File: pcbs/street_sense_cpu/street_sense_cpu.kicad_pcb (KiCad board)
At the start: 2 copper layers, 20 parts, among them J1 Conn_01x08, J10 Conn_01x06, J11 Conn_01x09, J13 Conn_01x02, J14 Conn_01x02, J3 Conn_01x06, J4 Conn_01x04, J5 Conn_01x02, J6 Conn_01x02, J7 Conn_01x08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

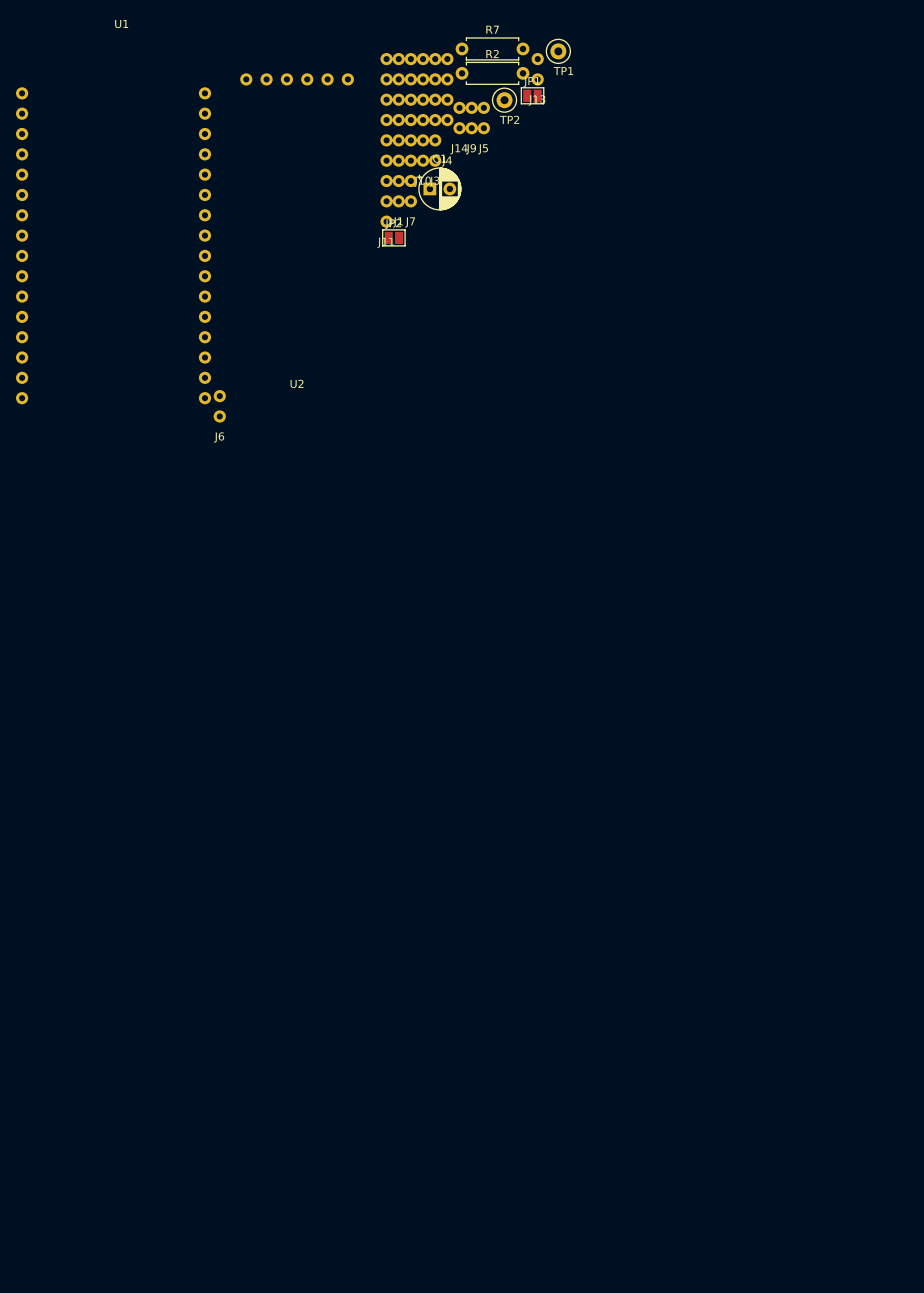
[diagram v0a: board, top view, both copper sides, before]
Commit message: updated CPU schematic
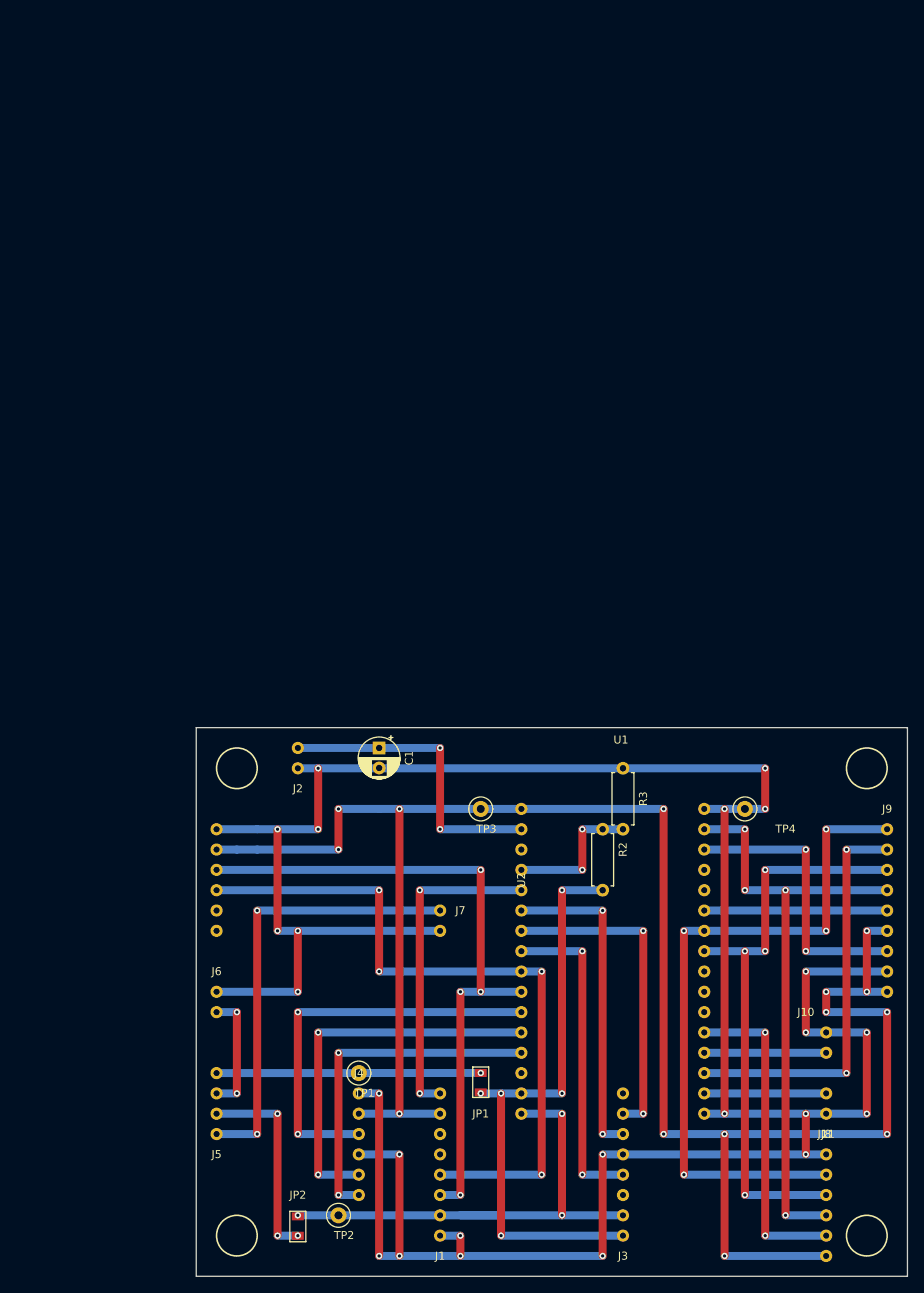
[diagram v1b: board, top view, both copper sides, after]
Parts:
- removed J13, J14: Conn_01x02, street-sense_footprints:connector_2pin
- removed R7: 100k, Resistor_THT:R_Axial_DIN0207_L6.3mm_D2.5mm_P7.62mm_Horizontal
- added J2: Conn_01x02, street_sense_footprints:connector_2pin, F.Cu at (114.3, 124.5)
- added J8: Conn_01x06, street_sense_footprints:connector_6pin, F.Cu at (180.3, 193.0)
- added R3: 100k, Resistor_THT:R_Axial_DIN0207_L6.3mm_D2.5mm_P7.62mm_Horizontal, F.Cu at (154.9, 129.5)
- added TP3: TestPoint, TestPoint:TestPoint_Loop_D2.50mm_Drill1.0mm, F.Cu at (137.2, 134.6)
- added TP4: TestPoint, TestPoint:TestPoint_Loop_D2.50mm_Drill1.0mm, F.Cu at (170.2, 134.6)
- J1: footprint street-sense_footprints:connector_8pin -> street_sense_footprints:connector_8pin
- J10: value Conn_01x06 -> Conn_01x02; footprint street-sense_footprints:connector_6pin -> street_sense_footprints:connector_2pin
- J11: value Conn_01x09 -> Conn_01x02; footprint street-sense_footprints:connector_9pin -> street_sense_footprints:connector_2pin
- J3: value Conn_01x06 -> Conn_01x08; footprint street-sense_footprints:connector_6pin -> street_sense_footprints:connector_8pin
- J4: value Conn_01x04 -> Conn_01x06; footprint street-sense_footprints:connector_4pin -> street_sense_footprints:connector_6pin
- J5: value Conn_01x02 -> Conn_01x04; footprint street-sense_footprints:connector_2pin -> street_sense_footprints:connector_4pin
- J6: footprint street-sense_footprints:connector_2pin -> street_sense_footprints:connector_2pin
- J7: value Conn_01x08 -> Conn_01x02; footprint street-sense_footprints:connector_8pin -> street_sense_footprints:connector_2pin
- J9: value Conn_01x02 -> Conn_01x09; footprint street-sense_footprints:connector_2pin -> street_sense_footprints:connector_9pin
- JP1, JP2: footprint Jumper:SolderJumper-2_P1.3mm_Open_Pad1.0x1.5mm -> street_sense_footprints:SolderJumper-2_P1.3mm_Open_Pad1.0x1.5mm
- R2: value 470k -> 68k
- U1: footprint street-sense_footprints:LolinD32 -> street_sense_footprints:LolinD32
- U2: footprint street-sense_footprints:DS3231_Module -> street_sense_footprints:DS3231_Module
- moved J4 147.5 mm to (121.9, 185.4), turned to 180 degrees
- moved TP2 140.9 mm to (119.4, 185.4)
- moved J11 140.5 mm to (180.3, 167.6)
- moved J10 138.8 mm to (180.3, 167.6), turned to 180 degrees
- moved J3 131.4 mm to (154.9, 167.6)
- moved TP1 130.1 mm to (121.9, 167.6)
- moved J1 129.4 mm to (132.1, 167.6)
- moved J9 126.7 mm to (188.0, 160.0), turned to 180 degrees
- moved JP2 125.3 mm to (114.3, 188.0), turned to 90 degrees
- moved J5 125.2 mm to (104.1, 165.1)
- moved JP1 122.3 mm to (137.2, 167.6), turned to 270 degrees
- moved U2 109.6 mm to (99.1, 147.3), turned to 90 degrees
- moved U1 109.1 mm to (154.9, 142.2)
- moved J7 106.5 mm to (132.1, 144.8)
- moved R2 96.1 mm to (152.4, 137.2), turned to 270 degrees
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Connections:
- J1 pad 1: Net-(J1-Pad1) -> /DRDY
- J1 pad 2: /PS_RX -> +3V3
- J1 pad 3: /PS_TX -> Net-(J1-Pad3)
- J1 pad 4: GND -> Net-(J1-Pad4)
- J1 pad 5: /PS_CTRL -> /SCL
- J1 pad 6: Net-(J1-Pad6) -> /SDA
- J1 pad 8: /USB -> GND
- J10 pad 1: +3V3 -> /ADVANCE
- J10 pad 2: /SD_CS -> GND
- J11 pad 1: +3V3 -> /SELECT
- J3 pad 1: /SCK -> Net-(J3-Pad1)
- J3 pad 2: /WS -> /PS_RX
- J3 pad 3: GND -> /PS_TX
- J3 pad 4: /SD -> GND
- J3 pad 5: +3V3 -> /PS_CTRL
- J3 pad 6: GND -> Net-(J3-Pad6)
- J4 pad 1: Net-(J4-Pad1) -> /M_SCK
- J4 pad 2: Net-(J4-Pad2) -> /M_WS
- J4 pad 3: Net-(J4-Pad3) -> GND
- J4 pad 4: Net-(J4-Pad4) -> /M_SD
- J5 pad 1: Net-(J4-Pad3) -> Net-(J5-Pad1)
- J5 pad 2: GND -> Net-(J5-Pad2)
- J6 pad 1: Net-(J4-Pad4) -> Net-(J5-Pad2)
- J7 pad 1: GND -> Net-(J5-Pad4)
- J7 pad 2: /BAT -> GND
- J9 pad 1: Net-(C1-Pad1) -> +3V3
- JP1 pad 1: Net-(J4-Pad1) -> Net-(J5-Pad1)
- JP2 pad 1: Net-(J4-Pad2) -> Net-(J5-Pad3)
- TP1 pad 1: /USB -> Net-(J5-Pad1)
- U1 pad 11: /SD -> /M_SD
- U1 pad 12: /WS -> /M_WS
- U1 pad 13: /SCK -> /M_SCK
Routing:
- net GND: track 0.00 -> 355.6 mm, vias 0 -> 27
- net +3V3: track 0.00 -> 248.9 mm, vias 0 -> 14
- net /SCL: track 0.00 -> 88.9 mm, vias 0 -> 4
- net /MISO: track 0.00 -> 86.4 mm, vias 0 -> 4
- net /SDA: track 0.00 -> 83.8 mm, vias 0 -> 4
- net /MOSI: track 0.00 -> 76.2 mm, vias 0 -> 4
- net /USB: track 0.00 -> 73.7 mm, vias 0 -> 5
- net /SCK: track 0.00 -> 73.7 mm, vias 0 -> 4
- net /BAT: track 0.00 -> 63.5 mm, vias 0 -> 3
- net Net-(J5-Pad4): track 0.00 -> 55.9 mm, vias 0 -> 2
- net /D_BL_CTRL: track 0.00 -> 50.8 mm, vias 0 -> 2
- net /M_SD: track 0.00 -> 50.8 mm, vias 0 -> 2
- net /M_WS: track 0.00 -> 48.3 mm, vias 0 -> 2
- net /M_SCK: track 0.00 -> 43.2 mm, vias 0 -> 2
- net /DRDY: track 0.00 -> 40.6 mm, vias 0 -> 2
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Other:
- board outline added: 88.9 x 68.6 mm
- net class Default: trace_width 0.25 -> 1
